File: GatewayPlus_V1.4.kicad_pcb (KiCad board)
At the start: 2 copper layers, 100 x 60 mm, 274 parts, among them IC1 MP1584EN, IC2 MP1584EN, J1 SWD_LOG, J10 USB_OTG, J11 USB_WIFI, J2 LTDC_LCD_FPC_40p, J3 Micro_SD_Card, J4 ESP Anten, J5 LoRa_Anten, J6 HR911105A, J7 RS485, J8 Conn_Jack-DC, J9 AudioJack, Q1 BC847, SW1 SW_Push, SW2 ESP_RESET, SW3 ESP_BOOT, U1 STM32F429IGTx, U10 USBLC6-2SC6, U11 USBLC6-2SC6, U2 IS42S16400J - HY57V641620E, U3 ESP32-C3, U4 W25Q32JVSS, U5 SX1278, U6 MASWSS0192, U7 LAN8720A, U8 MAX485E, U9 ES8388, Y1 25MHz, Y2 40MHz, Y3 32MHz, Y4 25MHz, Y5 32.768KHz

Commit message: Fix some bug.
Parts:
- moved J9 0.58 mm to (136.6, 72.2)
- moved C42 0.34 mm to (131.3, 111.5)
- moved C39 0.33 mm to (130.0, 111.5)
- moved L2 0.33 mm to (131.3, 114.4)
- moved C126 0.32 mm to (130.0, 114.4)
- moved C44 0.32 mm to (128.7, 114.4)
- moved D1 0.29 mm to (98.2, 75.1)
- moved C34 0.29 mm to (133.0, 112.4)
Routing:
- net GND: track 556.0 -> 536.2 mm, vias 98 -> 97
- net +3.3V: track 648.5 -> 634.5 mm, vias 57 -> 64
- net STATUS LED: track 9.10 -> 6.56 mm
- net /AUDIO/ROUT: track 11.4 -> 8.99 mm
- net Net-(U5-RXTX/RF_MOD): track 33.8 -> 31.7 mm
- net /MCU/SDIO_D3: track 27.1 -> 25.8 mm
- net USART6_TX: track 32.8 -> 33.8 mm
- net WiFi_RST: track 40.4 -> 41.3 mm
- net /LTDC TFT LCD/LTDC_R1: track 60.0 -> 60.9 mm
- net /LTDC TFT LCD/LTDC_R0: track 61.4 -> 62.3 mm
- net USART6_RX: track 34.8 -> 35.7 mm
- net /MCU/SDIO_CLK: track 18.1 -> 17.3 mm
- net /MCU/SDRAM_NBL0: track 21.8 -> 21.1 mm
- net /WIFI ESP32/F_D2: track 14.8 -> 14.1 mm
- net /LORA/LoRa_IRQ: track 50.0 -> 49.3 mm
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- added copper zone on F.Cu, net Net-(U3-VDD3P3_CPU)

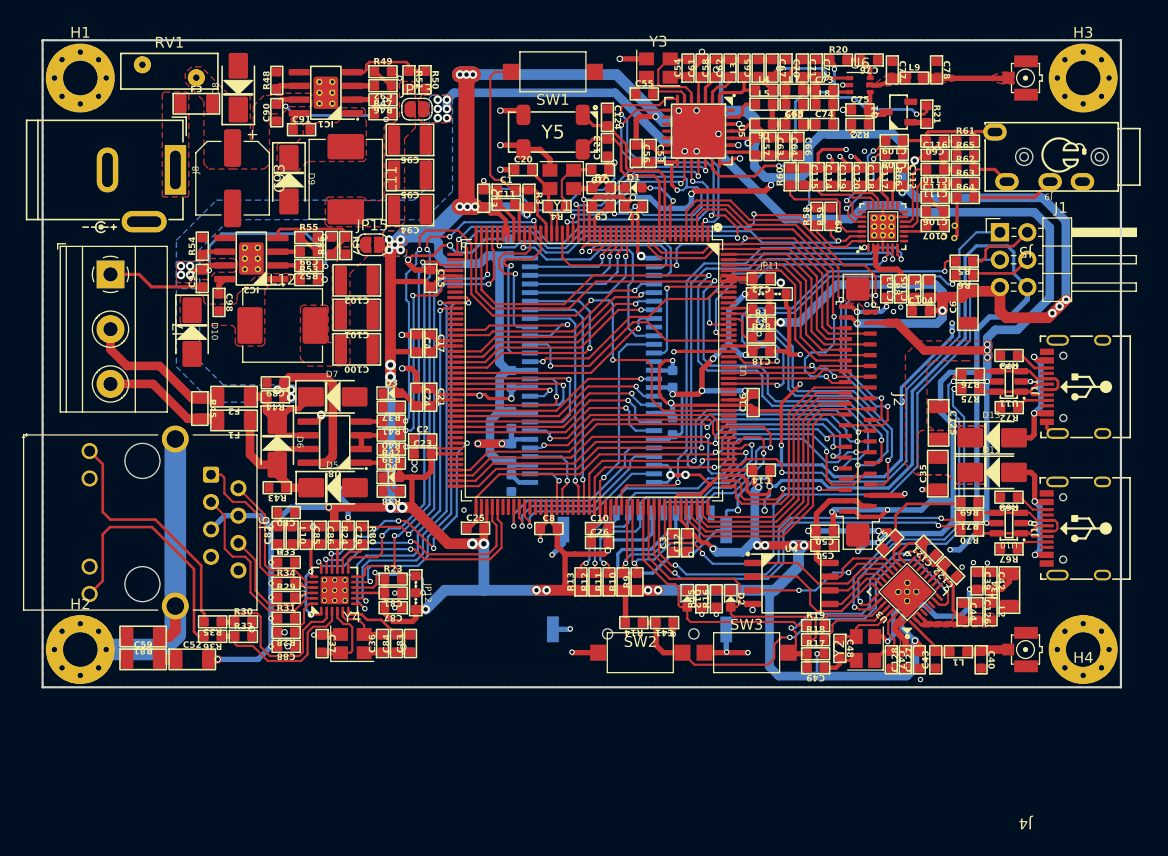
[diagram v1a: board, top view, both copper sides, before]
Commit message: Finish routing.
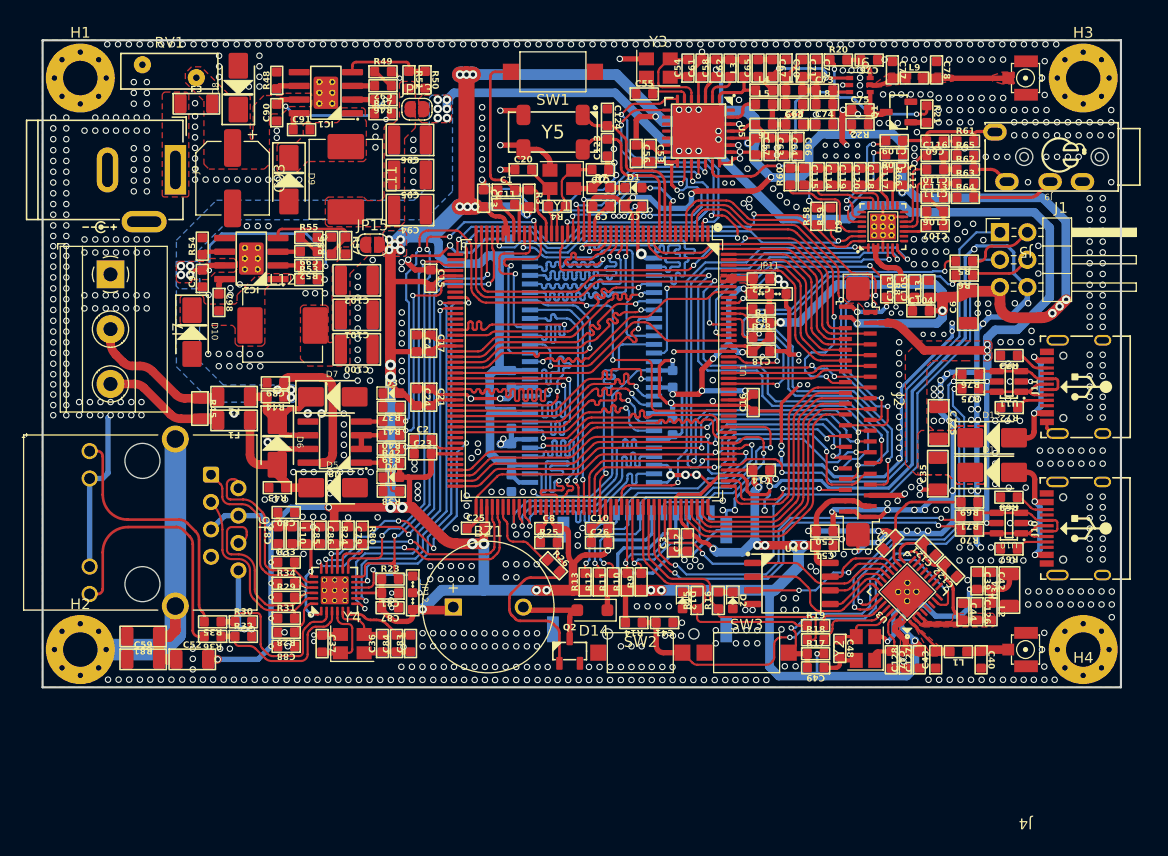
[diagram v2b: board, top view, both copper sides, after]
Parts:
- removed ? (x3): , 
- added BZ1: Buzzer, Buzzer_Beeper:MagneticBuzzer_ProSignal_ABT-410-RC, F.Cu at (81.4, 114.0)
- added D14: 1N4148W, Diode_SMD:D_SOD-123F, F.Cu at (94.3, 114.2)
- added Q2: BC847, Anh_Footprints:SOT23-3, F.Cu at (92.2, 118.0)
- added R25: 4k7, Anh_Footprints:R_0603, F.Cu at (90.3, 108.0)
- added R26: 1k, Anh_Footprints:R_0603, F.Cu at (90.7, 110.1)
- moved R15 0.46 mm to (104.0, 113.3)
- moved D12 0.46 mm to (102.7, 113.3)
- moved R10 0.39 mm to (97.6, 111.6)
- moved R11 0.39 mm to (96.3, 111.6)
- moved R9 0.39 mm to (98.9, 111.6)
- moved R12 0.39 mm to (95.0, 111.6)
- moved R13 0.39 mm to (93.7, 111.6)
- moved C81 0.28 mm to (75.6, 112.7)
- moved C87 0.28 mm to (75.6, 114.0)
- moved JP12 0.28 mm to (77.7, 112.7)
- moved R23 0.28 mm to (75.6, 111.4)
- moved D2 0.24 mm to (107.4, 113.3)
- moved R16 0.24 mm to (106.0, 113.3)
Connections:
- D12 pad 2: /MCU/USART1_TX -> +3.3V
- D2 pad 2: /MCU/USART1_RX -> +3.3V
- R15 pad 1: GND -> /MCU/USART1_TX
- R16 pad 1: GND -> /MCU/USART1_RX
- U1 pad 167: unconnected-(U1-PB8-Pad167) -> /LTDC TFT LCD/LCD_BACKGROUND_LED
- U1 pad 94: unconnected-(U1-PB14-Pad94) -> BUZZER
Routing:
- net Net-(Q2-B): track 0.00 -> 18.6 mm
- net /MCU/SDRAM_D0: track 5.48 -> 22.3 mm
- net /LTDC TFT LCD/LCD_BACKGROUND_LED: track 0.00 -> 16.6 mm, vias 0 -> 2
- net /MCU/SDRAM_A3: track 9.90 -> 22.2 mm
- net /MCU/SDRAM_D6: track 10.9 -> 22.2 mm
- net /MCU/SDRAM_A2: track 11.1 -> 22.2 mm
- net /MCU/SDRAM_D1: track 7.99 -> 18.8 mm
- net +3.3V: track 634.5 -> 644.9 mm, vias 64 -> 66
- net /MCU/SDRAM_A4: track 12.7 -> 22.3 mm
- net /MCU/SDRAM_A0: track 13.5 -> 22.2 mm
- net /MCU/SDRAM_D7: track 13.9 -> 22.1 mm
- net Net-(BZ1-+): track 0.00 -> 8.10 mm
- net /MCU/SDRAM_NRAS: track 14.5 -> 22.3 mm
- net /MCU/SDRAM_D5: track 14.8 -> 22.4 mm
- net BUZZER: track 0.00 -> 7.47 mm
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- added copper zone on F.Cu, net Net-(U3-LNA_IN)

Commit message: Finished Board.
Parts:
- moved J7 0.64 mm to (50.3, 83.1)
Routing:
- net +3.3V: track 644.9 -> 638.7 mm, vias 66 -> 67
- net GND: track 531.2 -> 528.0 mm, vias 943 -> 922
- net /LORA/LoRa_MISO: track 21.9 -> 20.0 mm
- net +5V: track 145.1 -> 143.8 mm
- net /RS485/A+: track 13.5 -> 12.3 mm
- net SWDIO: track 57.5 -> 56.7 mm
- net /MCU/USB_OTG_D_N: track 37.9 -> 37.1 mm
- net /MCU/USB_OTG_D_P: track 37.2 -> 36.4 mm
- net /RS485/B-: track 11.3 -> 10.6 mm
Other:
- outline, holes or cut-outs redrawn
- board text added: "+3V3"
- board text added: "+5V"
- board text added: "0"
- board text added: "1"
- board text added: "3V3"
- board text added: "A+"
- board text added: "Audio"
- board text added: "B-"
- board text added: "BOOT0"
- board text added: "CODEC"
- board text added: "DC 7-24V"
- board text added: "Design by Mai Văn Anh 20139059 Trần Đình Hoàng Anh 201390xx"
- board text added: "ETH"
- board text added: "GND"
- board text added: "LCD"
- board text added: "LOG"
- board text added: "LoRa"
- board text added: "LoRa Anten"
- board text added: "PHY ADDR"
- board text added: "RJ45"
- board text added: "RS485"
- board text added: "RUN"
- board text added: "SD CARD"
- board text added: "SDRAM"
- board text added: "STM32"
- board text added: "SWCLK"
- board text added: "SWD"
- board text added: "SWDIO"
- board text added: "U6 RX"
- board text added: "U6 TX"
- board text added: "USB OTG"
- board text added: "USB WiFi"
- board text added: "WiFi"
- board text added: "WiFi Anten"

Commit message: Finished Board.
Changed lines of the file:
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@@
   (arc (start 72.7 109) (mid 72.905061 108.915061) (end 72.99 108.71) (width 0.2) (layer "F.Cu") (net 261))
   (arc (start 71.19 109.34) (mid 71.289584 109.099584) (end 71.53 109) (width 0.2) (layer "F.Cu") (net 261))
+  (segment (start 54.155 116.685) (end 54.823219 116.685) (width 1) (layer "F.Cu") (net 263))
   (segment (start 54.155 116.685) (end 54.155 118.81) (width 1) (layer "F.Cu") (net 263))
-  (segment (start 55.6625 116.1075) (end 55.085 116.685) (width 1) (layer "F.Cu") (net 263))
-  (segment (start 55.085 116.685) (end 54.155 116.685) (width 1) (layer "F.Cu") (net 263))
   (segment (start 54.155 118.81) (end 55.755 118.81) (width 1) (layer "F.Cu") (net 263))
-  (segment (start 55.6625 113.865) (end 55.6625 116.1075) (width 1) (layer "F.Cu") (net 263))
+  (segment (start 55.6625 113.865) (end 55.6625 115.845719) (width 1) (layer "F.Cu") (net 263))
+  (arc (start 55.6625 115.845719) (mid 55.41668 116.43918) (end 54.823219 116.685) (width 1) (layer "F.Cu") (net 263))
   (segment (start 54.21 117.9) (end 46.85 117.9) (width 2) (layer "B.Cu") (net 263))
   (segment (start 55.6625 98.375) (end 55.6625 113.865) (width 2) (layer "B.Cu") (net 263))
